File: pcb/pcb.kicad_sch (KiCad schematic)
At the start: 2 parts, among them CN1 1x3, SW1 switch_3x6

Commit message: continued work on schematic
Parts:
- added CN2, CN3, CN4: 1x8, symbol pin_headers:1x8
- added CN5: 1x4, symbol pin_headers:1x4
- added CN6, CN7: 1x2, symbol pin_headers:1x2
- added D1: LED, SMT:0603, symbol generic:LED
- added F1: F, SMT:0603, symbol generic:fuse
- added R1: 1k, SMT:0603, symbol generic:R
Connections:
- net Battery: now also CN5.2
- net CAN/CAN_H: now also CN5.4
- net CAN/CAN_L: now also CN5.3
- net GND: now also CN4.1, CN4.2, CN4.3, CN4.4, CN4.5, CN4.6, CN4.7, CN4.8, CN5.1, CN6.2, CN7.1, D1.2 (K)
- net MCU/CH1: now also CN2.1
- net MCU/CH2: now also CN2.2
- net MCU/CH3: now also CN2.3
- net MCU/CH4: now also CN2.4
- net MCU/CH5: now also CN2.5
- net MCU/CH6: now also CN2.6
- net MCU/CH7: now also CN2.7
- net MCU/CH8: now also CN2.8
- new net: D1.1 (A), R1.1
- new net: CN6.1, F1.1
- new net MCU/status: R1.2
- new net Servo VCC: CN3.1, CN3.2, CN3.3, CN3.4, CN3.5, CN3.6, CN3.7, CN3.8, CN7.2
- new net power supply/+: F1.2
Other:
- sheet MCU ports: added status; removed none
- sheet power supply ports: added +; removed none
- note added: "30 A minifuse"
- note added: "ESC power jumper"
- note added: "Servo header"
- note added: "XT-60 Male"
- note removed: "1759033"
- moved on the sheet: CN1, SW1

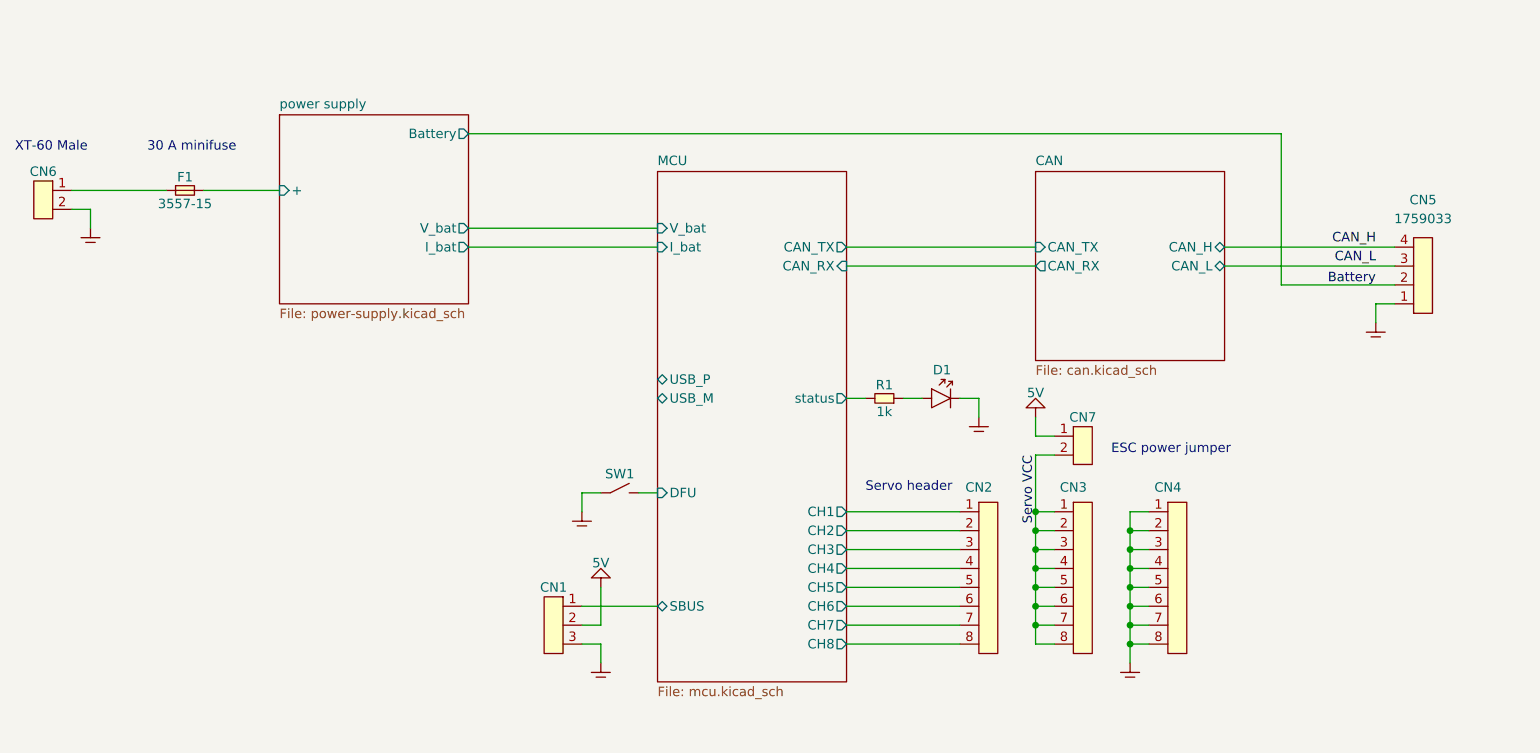
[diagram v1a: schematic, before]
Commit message: changed mcu layout to allow all desired features. added stm32 to schematic
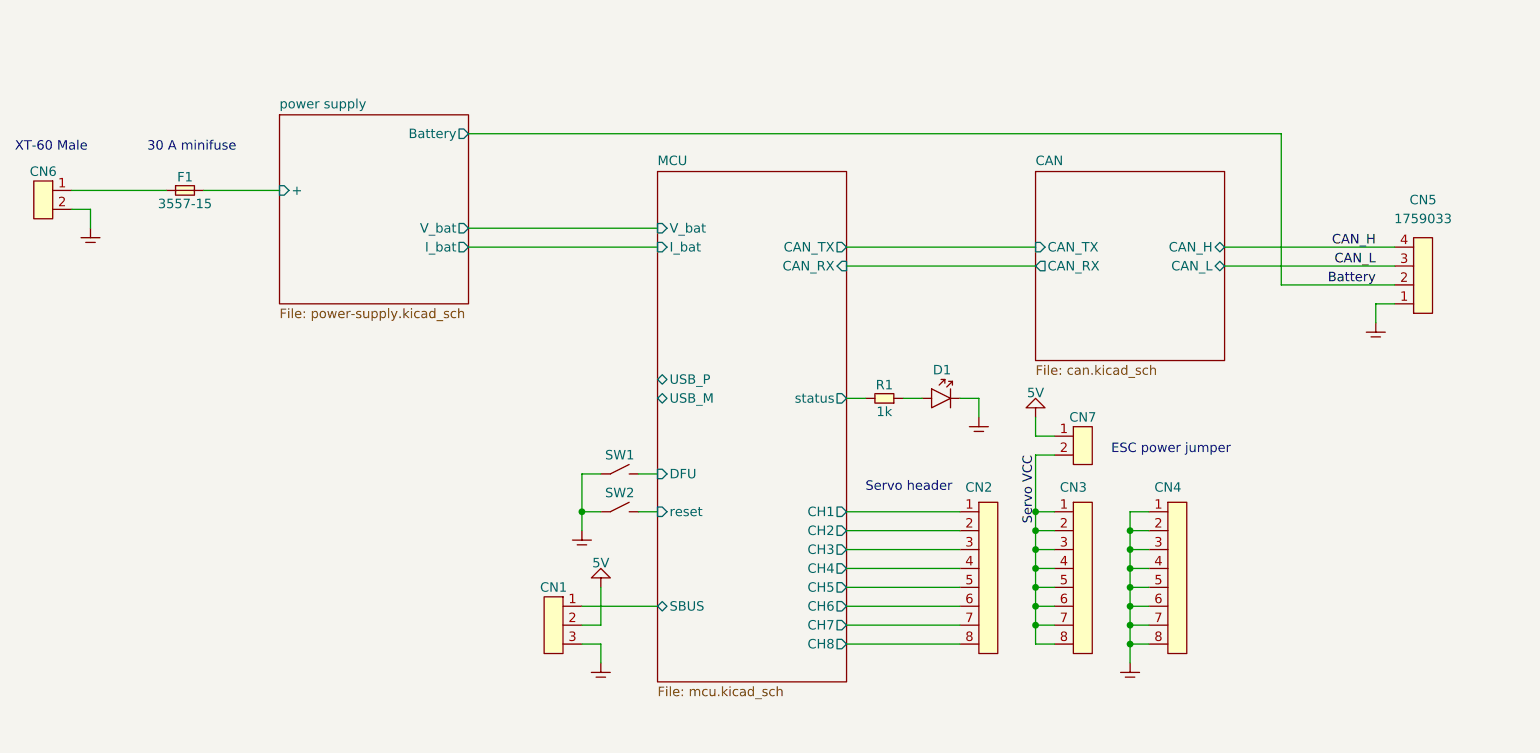
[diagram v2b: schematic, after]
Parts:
- added SW2: switch_3x4, buttons:sw_3x4, symbol switches:switch_3x4
- SW1: value switch_3x6 -> switch_3x4; footprint buttons:sw_3x6 -> buttons:sw_3x4; symbol switches:switch_3x6 -> switches:switch_3x4
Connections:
- net CAN/CAN_H is gone; now on net CAN_H: CN5.4
- net CAN/CAN_L is gone; now on net CAN_L: CN5.3
- net GND: now also SW1.2, SW2.1, SW2.2
- net MCU/DFU: now also SW1.3, SW1.4; no longer SW1.2
- new net MCU/reset: SW2.3, SW2.4
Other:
- sheet MCU ports: added reset; removed none
- moved on the sheet: SW1
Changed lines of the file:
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@@
 (kicad_sch (version 20230121) (generator eeschema)
   (paper "A4")
+  (junction (at 129.54 121.92) (diameter 0) (color 0 0 0 0)
+  )
   (junction (at 190.5 137.16) (diameter 0) (color 0 0 0 0)
   )
@@
     (stroke (width 0) (type default))
   )
-  (wire (pts (xy 129.54 119.38) (xy 132.08 119.38))
+  (wire (pts (xy 129.54 116.84) (xy 132.08 116.84))
     (stroke (width 0) (type default))
   )
@@
     (stroke (width 0) (type default))
   )
-  (wire (pts (xy 137.16 119.38) (xy 139.7 119.38))
+  (wire (pts (xy 137.16 116.84) (xy 139.7 116.84))
     (stroke (width 0) (type default))
   )
@@
     (stroke (width 0) (type default))
   )
+  (wire (pts (xy 129.54 121.92) (xy 132.08 121.92))
+    (stroke (width 0) (type default))
+  )
   (wire (pts (xy 203.2 127) (xy 203.2 124.46))
     (stroke (width 0) (type default))
   )
+  (wire (pts (xy 137.16 121.92) (xy 139.7 121.92))
+    (stroke (width 0) (type default))
+  )
   (wire (pts (xy 193.04 114.3) (xy 190.5 114.3))
     (stroke (width 0) (type default))
   )
-  (wire (pts (xy 129.54 121.92) (xy 129.54 119.38))
+  (wire (pts (xy 129.54 124.46) (xy 129.54 121.92))
     (stroke (width 0) (type default))
   )
@@
   )
   (wire (pts (xy 132.08 137.16) (xy 132.08 132.08))
+    (stroke (width 0) (type default))
+  )
+  (wire (pts (xy 129.54 121.92) (xy 129.54 116.84))
     (stroke (width 0) (type default))
   )
@@
     (effects (font (size 1.27 1.27)) (justify right bottom))
   )
-  (label "CAN_L" (at 236.251 88.6212 180) (fields_autoplaced)
+  (label "CAN_L" (at 236.22 88.9 180) (fields_autoplaced)
     (effects (font (size 1.27 1.27)) (justify right bottom))
   )
-  (label "CAN_H" (at 236.251 86.0812 180) (fields_autoplaced)
+  (label "CAN_H" (at 236.22 86.36 180) (fields_autoplaced)
     (effects (font (size 1.27 1.27)) (justify right bottom))
   )
@@
     )
   )
-  (symbol (lib_id "switches:switch_3x6") (at 134.62 119.38 0) (unit 1)
-    (in_bom yes) (on_board yes) (dnp no) (fields_autoplaced)
-    (property "Reference" "SW1" (at 134.62 116.84 0)
+  (symbol (lib_id "switches:switch_3x4") (at 134.62 116.84 0) (unit 1)
+    (in_bom yes) (on_board yes) (dnp no) (fields_autoplaced)
+    (property "Reference" "SW1" (at 134.62 114.3 0)
       (effects (font (size 1.27 1.27)))
     )
-    (property "Value" "switch_3x6" (at 134.62 116.84 0)
-      (effects (font (size 1.27 1.27)) hide)
-    )
-    (property "Footprint" "buttons:sw_3x6" (at 134.62 120.65 0)
-      (effects (font (size 1.27 1.27)) hide)
-    )
-    (property "Datasheet" "" (at 134.62 119.38 0)
-      (effects (font (size 1.27 1.27)) hide)
-    )
-    (pin "1")
-    (pin "2")
+    (property "Value" "switch_3x4" (at 134.62 114.3 0)
+      (effects (font (size 1.27 1.27)) hide)
+    )
+    (property "Footprint" "buttons:sw_3x4" (at 134.62 118.11 0)
+      (effects (font (size 1.27 1.27)) hide)
+    )
+    (property "Datasheet" "" (at 134.62 116.84 0)
+      (effects (font (size 1.27 1.27)) hide)
+    )
+    (pin "1")
+    (pin "2")
+    (pin "3")
+    (pin "4")
     (instances
       (project "pcb"
@@
     )
   )
-  (symbol (lib_id "generic:GND") (at 129.54 121.92 0) (unit 1)
-    (in_bom yes) (on_board yes) (dnp no) (fields_autoplaced)
-    (property "Reference" "GND01" (at 133.35 120.65 0)
-      (effects (font (size 1.27 1.27)) hide)
-    )
-    (property "Value" "GND" (at 133.35 121.92 0)
-      (effects (font (size 1.27 1.27)) hide)
-    )
-    (property "Footprint" "" (at 129.54 121.92 0)
-      (effects (font (size 1.27 1.27)) hide)
-    )
-    (property "Datasheet" "" (at 129.54 121.92 0)
+  (symbol (lib_id "switches:switch_3x4") (at 134.62 121.92 0) (unit 1)
+    (in_bom yes) (on_board yes) (dnp no)
+    (property "Reference" "SW2" (at 134.62 119.38 0)
+      (effects (font (size 1.27 1.27)))
+    )
+    (property "Value" "switch_3x4" (at 134.62 119.38 0)
+      (effects (font (size 1.27 1.27)) hide)
+    )
+    (property "Footprint" "buttons:sw_3x4" (at 134.62 123.19 0)
+      (effects (font (size 1.27 1.27)) hide)
+    )
+    (property "Datasheet" "" (at 134.62 121.92 0)
+      (effects (font (size 1.27 1.27)) hide)
+    )
+    (pin "1")
+    (pin "2")
+    (pin "3")
+    (pin "4")
+    (instances
+      (project "pcb"
+        (path "/6bb3bad6-1a89-4624-b34d-6ddda7dd16d2/19469851-aeaf-466c-9786-c0d0ae531cf4"
+          (reference "SW2") (unit 1)
+        )
+        (path "/6bb3bad6-1a89-4624-b34d-6ddda7dd16d2"
+          (reference "SW2") (unit 1)
+        )
+      )
+    )
+  )
+  (symbol (lib_id "generic:GND") (at 129.54 124.46 0) (unit 1)
+    (in_bom yes) (on_board yes) (dnp no) (fields_autoplaced)
+    (property "Reference" "GND01" (at 133.35 123.19 0)
+      (effects (font (size 1.27 1.27)) hide)
+    )
+    (property "Value" "GND" (at 133.35 124.46 0)
+      (effects (font (size 1.27 1.27)) hide)
+    )
+    (property "Footprint" "" (at 129.54 124.46 0)
+      (effects (font (size 1.27 1.27)) hide)
+    )
+    (property "Datasheet" "" (at 129.54 124.46 0)
       (effects (font (size 1.27 1.27)) hide)
     )
@@
       (effects (font (size 1.27 1.27)) (justify left))
     )
-    (pin "DFU" input (at 139.7 119.38 180)
+    (pin "DFU" input (at 139.7 116.84 180)
       (effects (font (size 1.27 1.27)) (justify left))
     )
@@
       (effects (font (size 1.27 1.27)) (justify right))
     )
-    (instances
+    (pin "reset" input (at 139.7 121.92 180)
+      (effects (font (size 1.27 1.27)) (justify left))
+    )
+    (instances

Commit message: schematic mostly done
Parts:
- added CN10: 1x2, symbol pin_headers:1x2
- added CN8: ~, USB:USB4105-GF-A, symbol connectors:USB4105-GF-A
- added R12, R13: 5k1, SMT:0603, symbol generic:R
- added R14: 120R, SMT:0603, symbol generic:R
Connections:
- net CAN_H: now also R14.2
- net CAN_L: now also CN10.2
- net GND: now also CN8.A1 (GND), CN8.A4 (VBUS), CN8.B1 (GND), CN8.B4 (VBUS), CN8.S1 (SHLD), CN8.S2 (SHLD), CN8.S3 (SHLD), CN8.S4 (SHLD), R12.2, R13.2
- net MCU/USB_M: now also CN8.A7 (D1N), CN8.B7 (DN2)
- net MCU/USB_P: now also CN8.A6 (D1P), CN8.B6 (DP2)
- new net: CN10.1, R14.1
- new net: CN8.A5 (CC1), R13.1
- new net: CN8.B5 (CC2), R12.1
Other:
- note added: "Termination selector"
- title: (none) -> CAN bus to RC servo adapter
- moved on the sheet: CN5

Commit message: started work on layout
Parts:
- CN10, CN7: footprint (none) -> pin_headers:1x2
- CN2, CN3, CN4: footprint (none) -> pin_headers:1x8
- F1: footprint SMT:0603 -> (none)
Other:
- note added: "5V is GND for some reason"
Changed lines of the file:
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@@
   (title_block
     (title "CAN bus to RC servo adapter")
-    (date "2024-01-10")
+    (date "2024-01-14")
     (rev "0")
     (comment 1 "User interfaces")
@@
     (effects (font (size 1.27 1.27)) (justify left bottom))
   )
+  (text "5V is GND for some reason" (at 109.22 63.5 0)
+    (effects (font (size 5 5)) (justify left bottom))
+  )
   (text "ESC power jumper" (at 200.66 114.3 0)
     (effects (font (size 1.27 1.27)) (justify left bottom))
@@
   (symbol (lib_id "generic:5V") (at 88.9 111.76 0) (unit 1)
     (in_bom yes) (on_board yes) (dnp no)
-    (property "Reference" "5V04" (at 92.71 110.49 0)
+    (property "Reference" "#5V04" (at 92.71 110.49 0)
       (effects (font (size 1.27 1.27)) hide)
     )
@@
       (project "pcb"
         (path "/6bb3bad6-1a89-4624-b34d-6ddda7dd16d2"
-          (reference "5V04") (unit 1)
+          (reference "#5V04") (unit 1)
         )
       )
@@
       (effects (font (size 1.27 1.27)) hide)
     )
-    (property "Footprint" "" (at 231.14 78.74 0)
+    (property "Footprint" "pin_headers:1x2" (at 231.14 78.74 0)
       (effects (font (size 1.27 1.27)) hide)
     )
@@
   (symbol (lib_id "generic:GND") (at 132.08 142.24 0) (unit 1)
     (in_bom yes) (on_board yes) (dnp no) (fields_autoplaced)
-    (property "Reference" "GND07" (at 135.89 140.97 0)
+    (property "Reference" "#GND07" (at 135.89 140.97 0)
       (effects (font (size 1.27 1.27)) hide)
     )
@@
       (project "pcb"
         (path "/6bb3bad6-1a89-4624-b34d-6ddda7dd16d2"
-          (reference "GND07") (unit 1)
+          (reference "#GND07") (unit 1)
         )
       )
@@
       (effects (font (size 1.27 1.27)) hide)
     )
-    (property "Footprint" "" (at 193.04 121.92 0)
+    (property "Footprint" "pin_headers:1x8" (at 193.04 121.92 0)
       (effects (font (size 1.27 1.27)) hide)
     )
@@
   (symbol (lib_id "generic:GND") (at 129.54 124.46 0) (unit 1)
     (in_bom yes) (on_board yes) (dnp no) (fields_autoplaced)
-    (property "Reference" "GND01" (at 133.35 123.19 0)
+    (property "Reference" "#GND01" (at 133.35 123.19 0)
       (effects (font (size 1.27 1.27)) hide)
     )
@@
       (project "pcb"
         (path "/6bb3bad6-1a89-4624-b34d-6ddda7dd16d2"
-          (reference "GND01") (unit 1)
+          (reference "#GND01") (unit 1)
         )
       )
@@
   (symbol (lib_id "generic:GND") (at 203.2 142.24 0) (unit 1)
     (in_bom yes) (on_board yes) (dnp no) (fields_autoplaced)
-    (property "Reference" "GND09" (at 207.01 140.97 0)
+    (property "Reference" "#GND09" (at 207.01 140.97 0)
       (effects (font (size 1.27 1.27)) hide)
     )
@@
       (project "pcb"
         (path "/6bb3bad6-1a89-4624-b34d-6ddda7dd16d2"
-          (reference "GND09") (unit 1)
+          (reference "#GND09") (unit 1)
         )
       )
@@
       (effects (font (size 1.27 1.27)) hide)
     )
-    (property "Footprint" "" (at 205.74 121.92 0)
+    (property "Footprint" "pin_headers:1x8" (at 205.74 121.92 0)
       (effects (font (size 1.27 1.27)) hide)
     )
@@
       (effects (font (size 1.27 1.27)) hide)
     )
-    (property "Footprint" "" (at 180.34 121.92 0)
+    (property "Footprint" "pin_headers:1x8" (at 180.34 121.92 0)
       (effects (font (size 1.27 1.27)) hide)
     )
@@
         )
         (path "/6bb3bad6-1a89-4624-b34d-6ddda7dd16d2"
-          (reference "GND08") (unit 1)
+          (reference "#GND08") (unit 1)
         )
       )
@@
   (symbol (lib_id "generic:GND") (at 182.88 109.22 0) (unit 1)
     (in_bom yes) (on_board yes) (dnp no) (fields_autoplaced)
-    (property "Reference" "GND010" (at 186.69 107.95 0)
+    (property "Reference" "#GND010" (at 186.69 107.95 0)
       (effects (font (size 1.27 1.27)) hide)
     )
@@
       (project "pcb"
         (path "/6bb3bad6-1a89-4624-b34d-6ddda7dd16d2"
-          (reference "GND010") (unit 1)
+          (reference "#GND010") (unit 1)
         )
       )
@@
       (effects (font (size 1.27 1.27)) hide)
     )
-    (property "Footprint" "SMT:0603" (at 73.66 79.375 0)
+    (property "Footprint" "" (at 73.66 79.375 0)
       (effects (font (size 1.27 1.27)) hide)
     )
@@
   (symbol (lib_name "GND_1") (lib_id "generic:GND") (at 78.74 149.86 0) (unit 1)
     (in_bom yes) (on_board yes) (dnp no) (fields_autoplaced)
-    (property "Reference" "#GND01" (at 82.55 148.59 0)
+    (property "Reference" "#GND034" (at 82.55 148.59 0)
       (effects (font (size 1.27 1.27)) hide)
     )
@@
       (project "pcb"
         (path "/6bb3bad6-1a89-4624-b34d-6ddda7dd16d2"
-          (reference "#GND01") (unit 1)
+          (reference "#GND034") (unit 1)
         )
       )
@@
   (symbol (lib_id "generic:5V") (at 190.5 109.22 0) (unit 1)
     (in_bom yes) (on_board yes) (dnp no)
-    (property "Reference" "5V03" (at 194.31 107.95 0)
+    (property "Reference" "#5V03" (at 194.31 107.95 0)
       (effects (font (size 1.27 1.27)) hide)
     )
@@
       (project "pcb"
         (path "/6bb3bad6-1a89-4624-b34d-6ddda7dd16d2"
-          (reference "5V03") (unit 1)
+          (reference "#5V03") (unit 1)
         )
       )
@@
   (symbol (lib_id "generic:GND") (at 63.5 83.82 0) (unit 1)
     (in_bom yes) (on_board yes) (dnp no) (fields_autoplaced)
-    (property "Reference" "GND016" (at 67.31 82.55 0)
+    (property "Reference" "#GND016" (at 67.31 82.55 0)
       (effects (font (size 1.27 1.27)) hide)
     )
@@
       (project "pcb"
         (path "/6bb3bad6-1a89-4624-b34d-6ddda7dd16d2"
-          (reference "GND016") (unit 1)
+          (reference "#GND016") (unit 1)
         )
       )
@@
       (effects (font (size 1.27 1.27)) hide)
     )
-    (property "Footprint" "" (at 193.04 111.76 0)
+    (property "Footprint" "pin_headers:1x2" (at 193.04 111.76 0)
       (effects (font (size 1.27 1.27)) hide)
     )
@@
   (symbol (lib_id "generic:5V") (at 132.08 132.08 0) (unit 1)
     (in_bom yes) (on_board yes) (dnp no)
-    (property "Reference" "5V02" (at 135.89 130.81 0)
+    (property "Reference" "#5V02" (at 135.89 130.81 0)
       (effects (font (size 1.27 1.27)) hide)
     )
@@
       (project "pcb"
         (path "/6bb3bad6-1a89-4624-b34d-6ddda7dd16d2"
-          (reference "5V02") (unit 1)
-        )
-      )
+          (reference "#5V02") (unit 1)
+        )
+      )

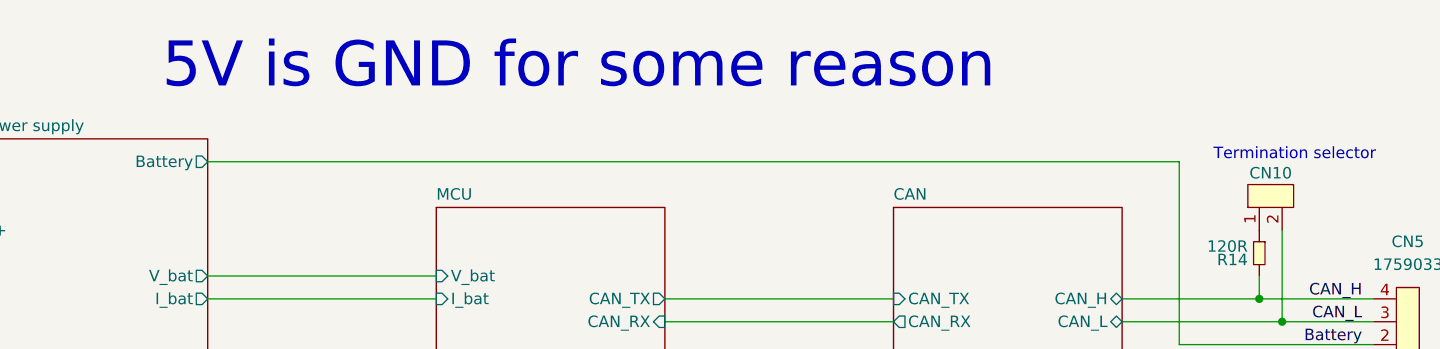
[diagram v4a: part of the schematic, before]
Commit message: fixed 5V being GND net
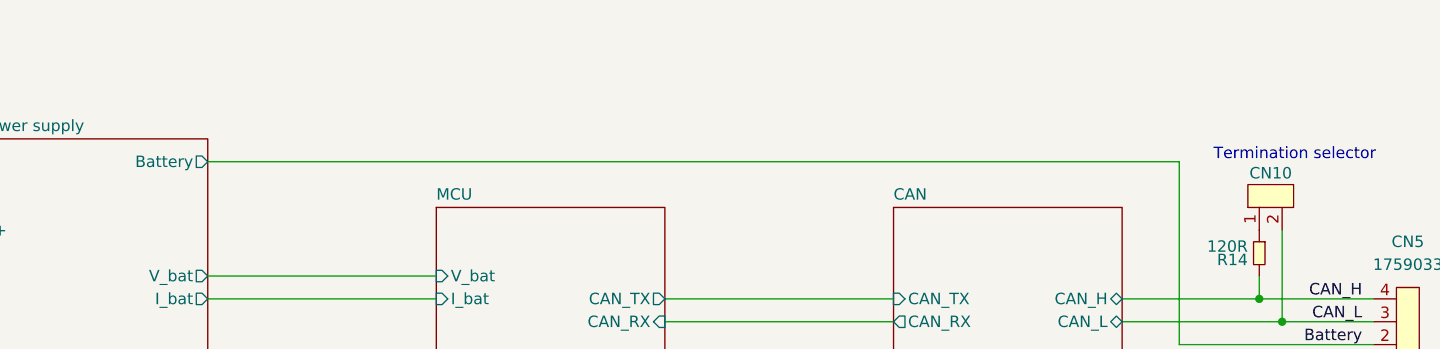
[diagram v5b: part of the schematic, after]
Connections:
- net GND: no longer CN1.2, CN7.1, CN8.A4 (VBUS), CN8.B4 (VBUS)
- new net 5V: CN1.2, CN7.1, CN8.A4 (VBUS), CN8.B4 (VBUS)
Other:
- note removed: "5V is GND for some reason"
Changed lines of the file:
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@@
+    (stroke (width 0) (type default))
+  )
+  (wire (pts (xy 190.5 111.76) (xy 193.04 111.76))
     (stroke (width 0) (type default))
   )
@@
     (stroke (width 0) (type default))
   )
+  (wire (pts (xy 190.5 109.22) (xy 190.5 111.76))
+    (stroke (width 0) (type default))
+  )
   (wire (pts (xy 132.08 139.7) (xy 132.08 142.24))
     (stroke (width 0) (type default))
@@
     (stroke (width 0) (type default))
   )
-  (wire (pts (xy 190.5 111.76) (xy 193.04 111.76))
-    (stroke (width 0) (type default))
-  )
   (wire (pts (xy 165.1 134.62) (xy 180.34 134.62))
     (stroke (width 0) (type default))
@@
   )
   (wire (pts (xy 190.5 121.92) (xy 193.04 121.92))
-    (stroke (width 0) (type default))
-  )
-  (wire (pts (xy 190.5 109.22) (xy 190.5 111.76))
     (stroke (width 0) (type default))
   )
@@
     (effects (font (size 1.27 1.27)) (justify left bottom))
   )
-  (text "5V is GND for some reason" (at 109.22 63.5 0)
-    (effects (font (size 5 5)) (justify left bottom))
-  )
   (text "ESC power jumper" (at 200.66 114.3 0)
